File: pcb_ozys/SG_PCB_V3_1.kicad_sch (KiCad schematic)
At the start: 0 parts

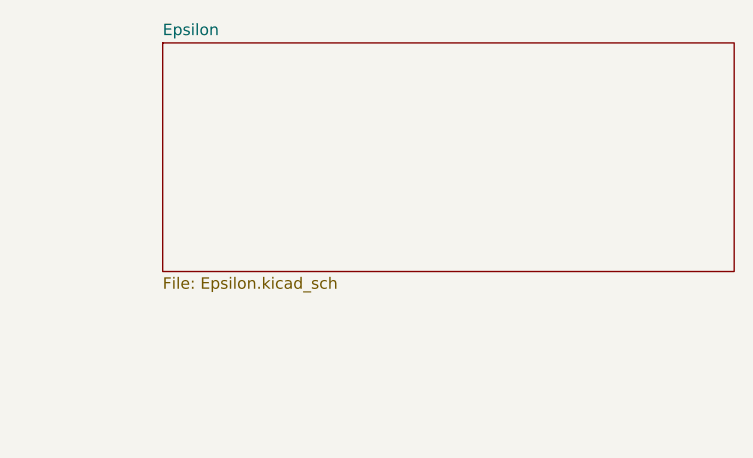
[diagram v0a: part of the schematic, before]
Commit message: Started PCBs fixed connectors
- Fixed Bypass on CAN
- Seperated SG connectors from 2x1 to 1x1
- Rough Draft of Epsilon
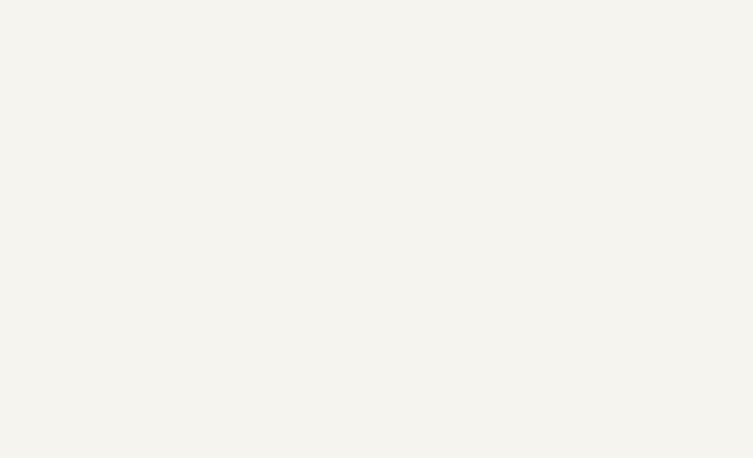
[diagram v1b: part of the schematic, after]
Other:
- removed sheet Epsilon
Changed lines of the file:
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@@
 	(paper "A4")
-	(sheet
-		(at 135.89 50.8)
-		(size 63.5 25.4)
-		(fields_autoplaced yes)
-		(stroke
-			(width 0.1524)
-			(type solid)
-		)
-		(fill
-			(color 0 0 0 0.0000)
-		)
-		(property "Sheetname" "Epsilon"
-			(at 135.89 50.0884 0)
-			(effects
-				(font
-					(size 1.27 1.27)
-				)
-				(justify left bottom)
-			)
-		)
-		(property "Sheetfile" "Epsilon.kicad_sch"
-			(at 135.89 76.7846 0)
-			(effects
-				(font
-					(size 1.27 1.27)
-				)
-				(justify left top)
-			)
-		)
-		(instances
-			(project "SG_PCB_V3_1"
-				(path "/c13c867e-6e7c-48dd-82ed-469b98ba6beb"
-					(page "3")
-				)
-			)
-		)
-	)
 	(sheet
 		(at 49.53 50.8)
